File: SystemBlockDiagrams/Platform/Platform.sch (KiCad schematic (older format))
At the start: 18 parts

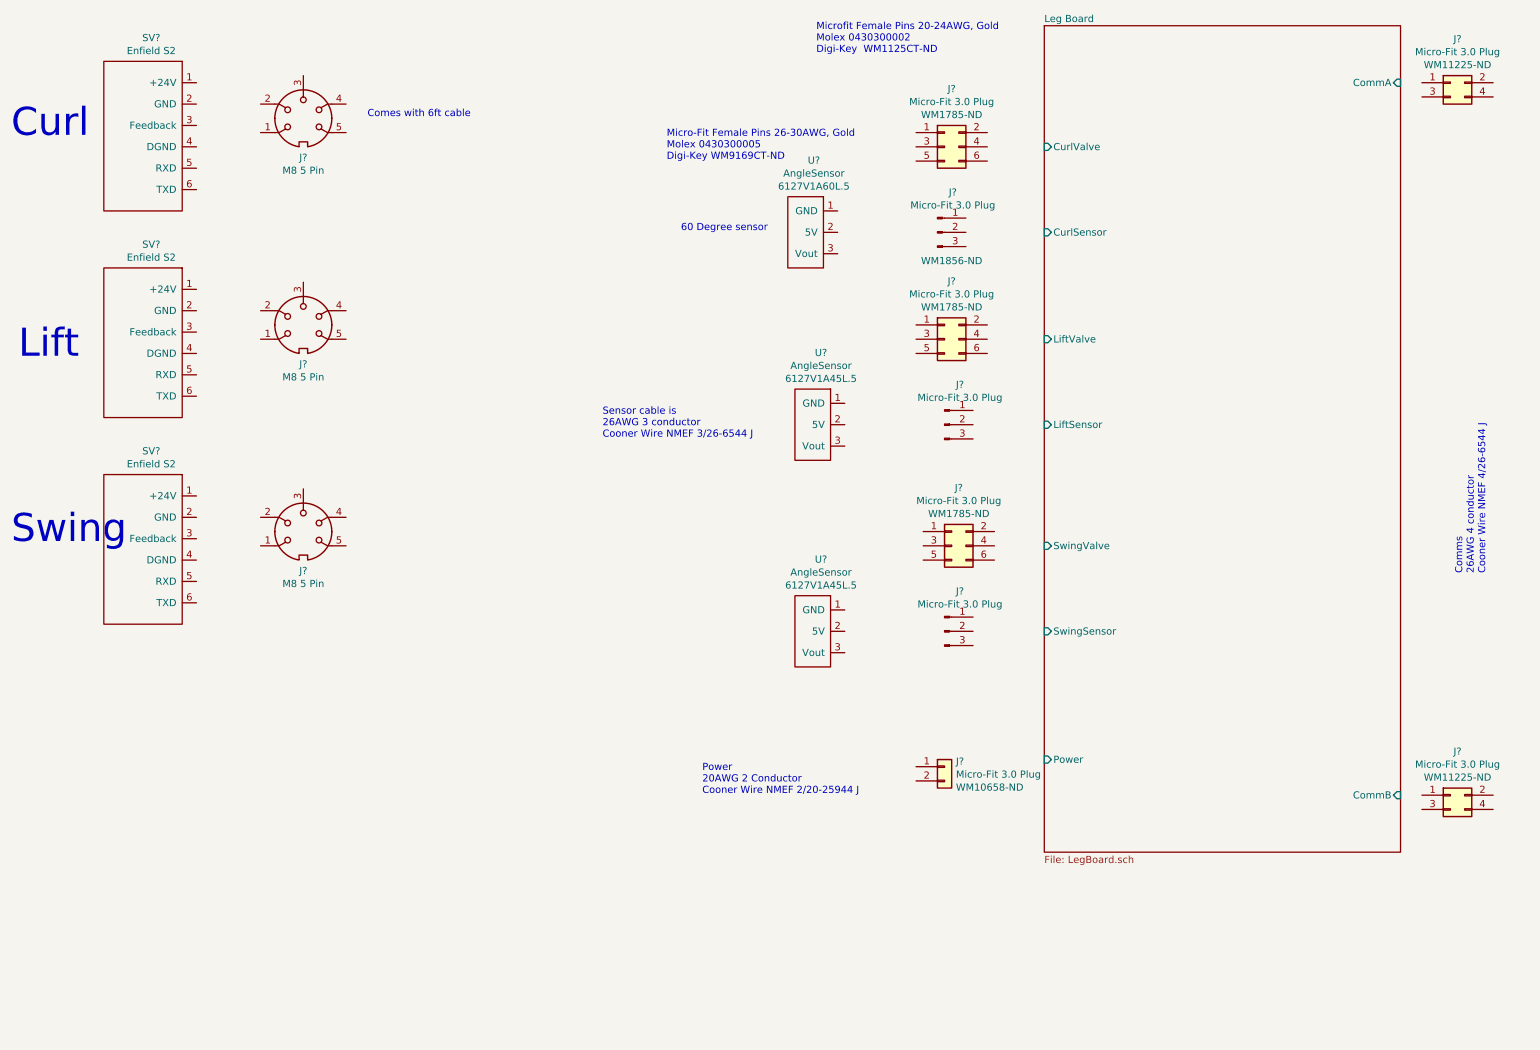
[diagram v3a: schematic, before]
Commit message: Update to show all legs on block diagram
Add radios to platform diagram
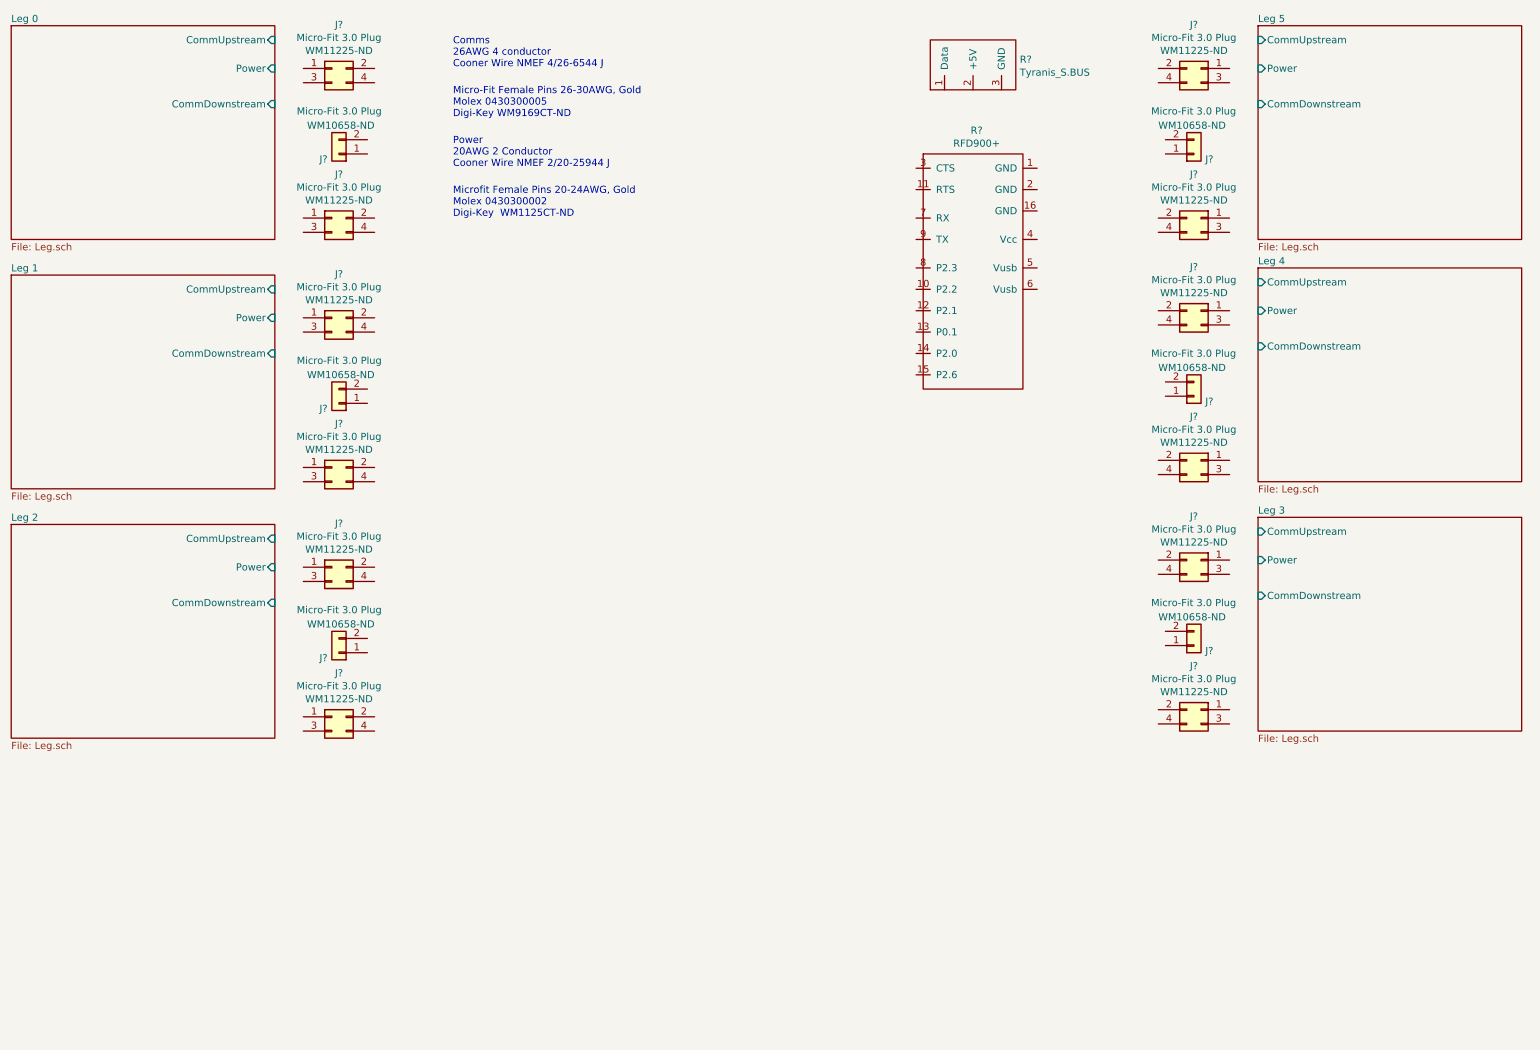
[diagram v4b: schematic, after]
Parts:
- removed J? (x3): Micro-Fit 3.0 Plug, symbol Connector_Generic:Conn_02x03_Odd_Even
- removed J? (x3): Micro-Fit 3.0 Plug, symbol Connector:Conn_01x03_Male
- removed J? (x3): M8 5 Pin, symbol Connector:DIN-5
- removed SV? (x3): Enfield S2, symbol Stomp:PneumaticServoValve
- removed U? (x3): AngleSensor, symbol Stomp:AngleSensor
- added J? (x10): Micro-Fit 3.0 Plug, symbol Connector_Generic:Conn_02x02_Odd_Even
- added J? (x5): Micro-Fit 3.0 Plug, symbol Connector_Generic:Conn_01x02
- added R?: Tyranis_S.BUS, symbol Stomp:Tyranis_S.BUS
- added R?: RFD900+, symbol Stomp:RFD900+
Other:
- note removed: "60 Degree sensor"
- note removed: "Comes with 6ft cable"
- note removed: "Curl"
- note removed: "Lift"
- note removed: "Sensor cable is\n26AWG 3 conductor\nCooner Wire NMEF 3/26-6544 J"
- note removed: "Swing"
- moved on the sheet: J?

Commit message: Start power distribution
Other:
- note added: "TODO:\n IMU\n IMU Connectors\n Telem Radio Connectors\n Ctrl radio connectors\n Pressure Sensor\n Pressure Sensor connectors\n"
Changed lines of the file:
@@
 $Descr A4 11693 8268
 encoding utf-8
-Sheet 1 3
+Sheet 1 15
 Title ""
 Date ""
@@
 	1    0    0    -1
 $EndComp
+Text Notes 4600 3000 0    50   ~ 0
+TODO:\n    IMU\n    IMU Connectors\n    Telem Radio Connectors\n    Ctrl radio connectors\n    Pressure Sensor\n    Pressure Sensor connectors\n
+$Sheet
+S 4900 4000 1450 2000
+U 5E269D05
+F0 "Power Distribution" 50
+F1 "PowerDistribution.sch" 50
+F2 "MCU_5V" I R 6350 4150 50
+F3 "MCU_GND" I R 6350 4250 50
+F4 "Ctrl_5V" I R 6350 4400 50
+F5 "Ctrl_GND" I R 6350 4500 50
+F6 "Telem_5V" I R 6350 4650 50
+F7 "Telem_GND" I R 6350 4750 50
+F8 "Pressure_5V" I R 6350 4900 50
+F9 "Pressure_GND" I R 6350 5050 50
+F10 "Leg0_24V" I L 4900 5200 50
+F11 "Leg0_GND" I L 4900 5300 50
+F12 "Leg1_24V" I L 4900 5450 50
+F13 "Leg1_GND" I L 4900 5550 50
+F14 "Leg2_24V" I L 4900 5700 50
+F15 "Leg2_GND" I L 4900 5800 50
+F16 "Leg3_GND" I R 6350 5800 50
+F17 "Leg3_24V" I R 6350 5700 50
+F18 "Leg4_GND" I R 6350 5550 50
+F19 "Leg4_24V" I R 6350 5450 50
+F20 "Leg5_GND" I R 6350 5300 50
+F21 "Leg5_24V" I R 6350 5200 50
+F22 "CAN_A" I L 4900 4150 50
+F23 "CAN_B" I L 4900 4250 50
+$EndSheet
 $EndSCHEMATC

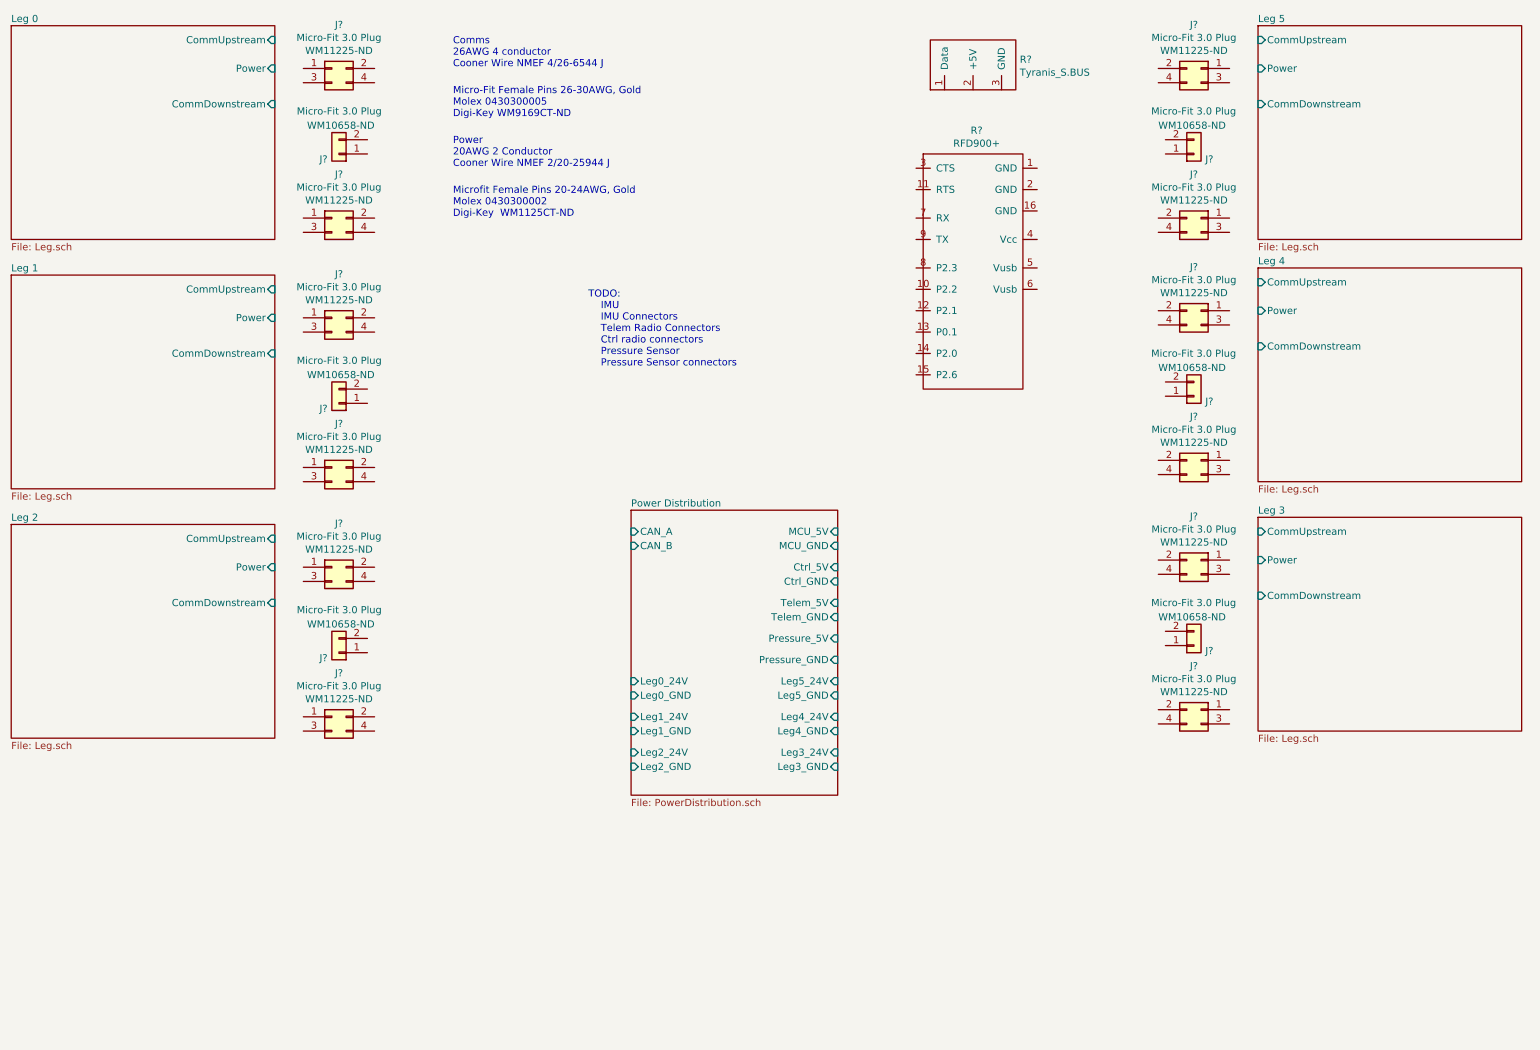
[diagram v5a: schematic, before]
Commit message: More platorm parts and connectors
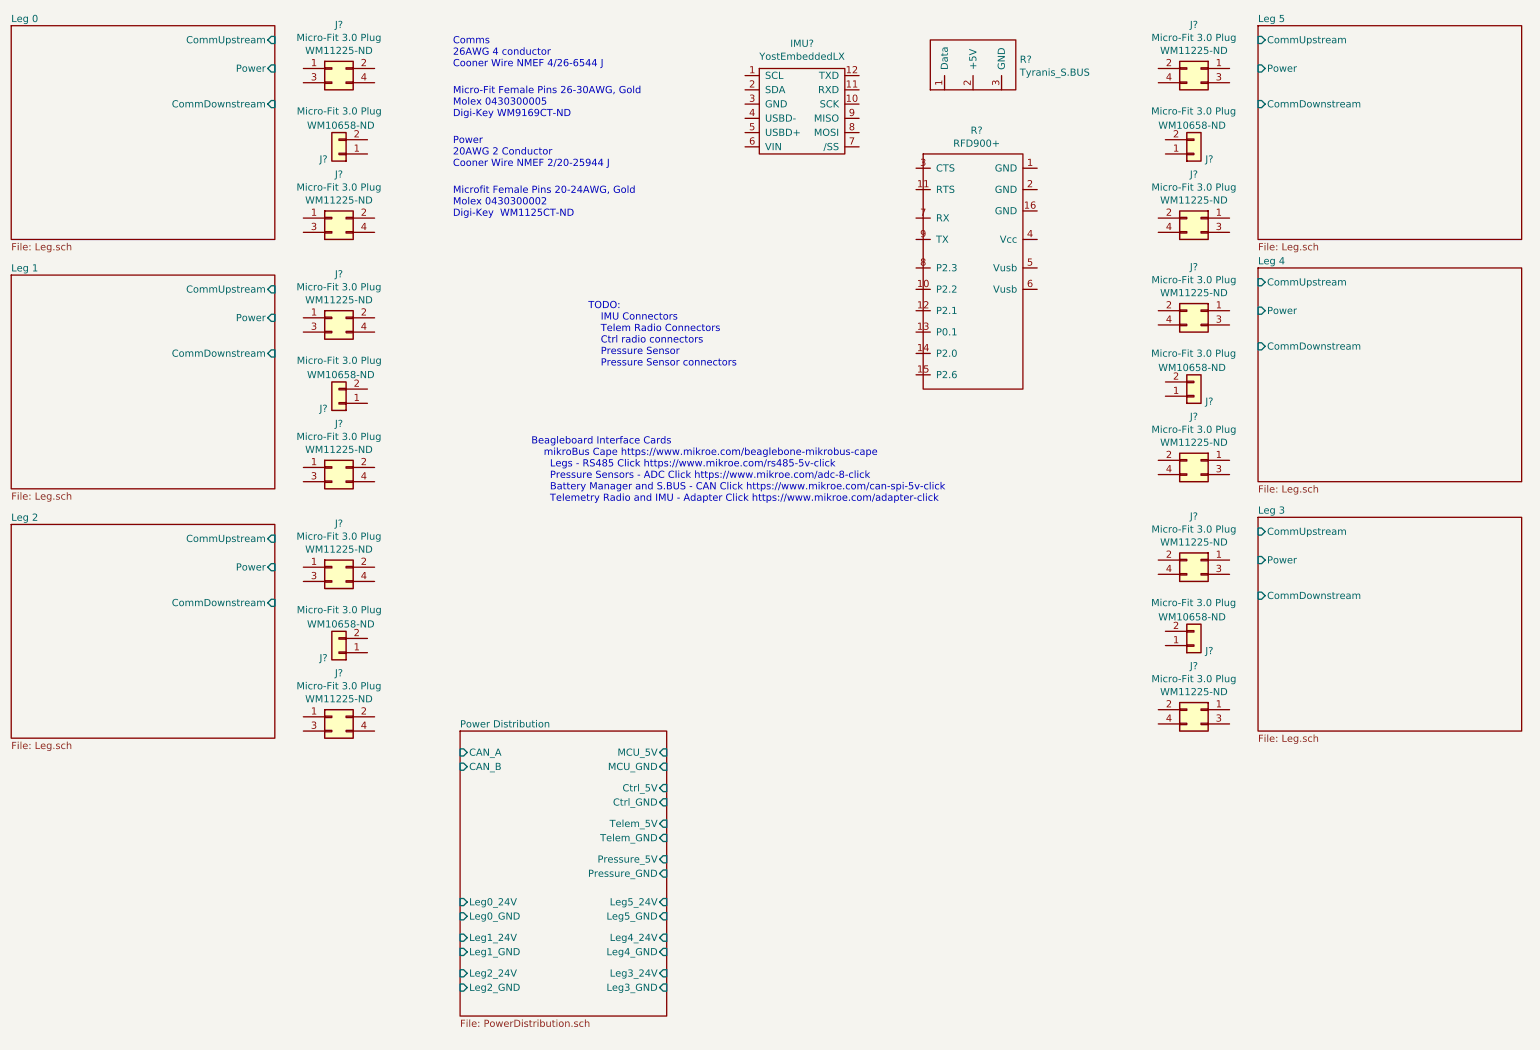
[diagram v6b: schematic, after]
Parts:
- added IMU?: YostEmbeddedLX, symbol Stomp:YostEmbeddedLX
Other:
- note added: "Beagleboard Interface Cards\n mikroBus Cape https://www.mikroe.com/beaglebone-mikrobus-cape\n Legs - RS485 Click https://www.mikroe.com/rs485-5v-click\n Pressure Sensors - ADC Click https://www.mikroe.com/adc-8-click\n Battery Manager and S.BUS - CAN Click https://www.mikroe.com/can-spi-5v-click\n Telemetry Radio and IMU - Adapter Click https://www.mikroe.com/adapter-click"
- note added: "TODO:\n IMU Connectors\n Telem Radio Connectors\n Ctrl radio connectors\n Pressure Sensor\n Pressure Sensor connectors\n"
- note removed: "TODO:\n IMU\n IMU Connectors\n Telem Radio Connectors\n Ctrl radio connectors\n Pressure Sensor\n Pressure Sensor connectors\n"
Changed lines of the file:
@@
 $EndComp
 Text Notes 4600 3000 0    50   ~ 0
-TODO:\n    IMU\n    IMU Connectors\n    Telem Radio Connectors\n    Ctrl radio connectors\n    Pressure Sensor\n    Pressure Sensor connectors\n
+TODO:\n    IMU Connectors\n    Telem Radio Connectors\n    Ctrl radio connectors\n    Pressure Sensor\n    Pressure Sensor connectors\n
 $Sheet
-S 4900 4000 1450 2000
+S 3700 5550 1450 2000
 U 5E269D05
 F0 "Power Distribution" 50
 F1 "PowerDistribution.sch" 50
-F2 "MCU_5V" I R 6350 4150 50
-F3 "MCU_GND" I R 6350 4250 50
-F4 "Ctrl_5V" I R 6350 4400 50
-F5 "Ctrl_GND" I R 6350 4500 50
-F6 "Telem_5V" I R 6350 4650 50
-F7 "Telem_GND" I R 6350 4750 50
-F8 "Pressure_5V" I R 6350 4900 50
-F9 "Pressure_GND" I R 6350 5050 50
-F10 "Leg0_24V" I L 4900 5200 50
-F11 "Leg0_GND" I L 4900 5300 50
-F12 "Leg1_24V" I L 4900 5450 50
-F13 "Leg1_GND" I L 4900 5550 50
-F14 "Leg2_24V" I L 4900 5700 50
-F15 "Leg2_GND" I L 4900 5800 50
-F16 "Leg3_GND" I R 6350 5800 50
-F17 "Leg3_24V" I R 6350 5700 50
-F18 "Leg4_GND" I R 6350 5550 50
-F19 "Leg4_24V" I R 6350 5450 50
-F20 "Leg5_GND" I R 6350 5300 50
-F21 "Leg5_24V" I R 6350 5200 50
-F22 "CAN_A" I L 4900 4150 50
-F23 "CAN_B" I L 4900 4250 50
+F2 "MCU_5V" I R 5150 5700 50
+F3 "MCU_GND" I R 5150 5800 50
+F4 "Ctrl_5V" I R 5150 5950 50
+F5 "Ctrl_GND" I R 5150 6050 50
+F6 "Telem_5V" I R 5150 6200 50
+F7 "Telem_GND" I R 5150 6300 50
+F8 "Pressure_5V" I R 5150 6450 50
+F9 "Pressure_GND" I R 5150 6550 50
+F10 "Leg0_24V" I L 3700 6750 50
+F11 "Leg0_GND" I L 3700 6850 50
+F12 "Leg1_24V" I L 3700 7000 50
+F13 "Leg1_GND" I L 3700 7100 50
+F14 "Leg2_24V" I L 3700 7250 50
+F15 "Leg2_GND" I L 3700 7350 50
+F16 "Leg3_GND" I R 5150 7350 50
+F17 "Leg3_24V" I R 5150 7250 50
+F18 "Leg4_GND" I R 5150 7100 50
+F19 "Leg4_24V" I R 5150 7000 50
+F20 "Leg5_GND" I R 5150 6850 50
+F21 "Leg5_24V" I R 5150 6750 50
+F22 "CAN_A" I L 3700 5700 50
+F23 "CAN_B" I L 3700 5800 50
 $EndSheet
+$Comp
+L Stomp:YostEmbeddedLX IMU?
+U 1 1 5E27BFDD
+P 6100 1200
+F 0 "IMU?" H 6100 1675 50  0000 C CNN
+F 1 "YostEmbeddedLX" H 6100 1584 50  0000 C CNN
+F 2 "" H 5950 1550 50  0001 C CNN
+F 3 "https://yostlabs.com/wp/wp-content/uploads/pdf/3-Space-Sensor-Users-Manual-Embedded-LX.pdf" H 5950 1550 50  0001 C CNN
+F 4 "Yost Labs" H 6100 1200 50  0001 C CNN "Supplier"
+F 5 "TSS_LX" H 6100 1200 50  0001 C CNN "Supplier Part Number"
+	1    6100 1200
+	1    0    0    -1
+$EndComp
+Text Notes 4200 3950 0    50   ~ 0
+Beagleboard Interface Cards\n    mikroBus Cape https://www.mikroe.com/beaglebone-mikrobus-cape\n      Legs - RS485 Click https://www.mikroe.com/rs485-5v-click\n      Pressure Sensors - ADC Click https://www.mikroe.com/adc-8-click\n      Battery Manager and S.BUS - CAN Click https://www.mikroe.com/can-spi-5v-click\n      Telemetry Radio and IMU - Adapter Click https://www.mikroe.com/adapter-click
 $EndSCHEMATC
